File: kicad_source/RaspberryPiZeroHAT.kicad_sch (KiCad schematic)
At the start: 45 parts, among them CN1 RASPI-IO, CN2 WE_691210910004, CN3 SPE-T1-STRM-90, CN4 SPE-T1-STRM-90, SW1 SS-3235S-L3, U1 LAN8651, Y1 X1E0000210808

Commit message: glued project together
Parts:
- removed C1, C10, C4, C6, C7, C8, C9: 100nF, Capacitor_SMD:C_0603_1608Metric, symbol Device:C_Small
- removed C11, C12: 220nF, Capacitor_SMD:C_0603_1608Metric, symbol Device:C_Small
- removed C13, C14: 10 uF, Capacitor_SMD:C_0603_1608Metric, symbol Device:C_Small
- removed C2, C3: 22pF, Capacitor_SMD:C_0603_1608Metric, symbol Device:C_Small
- removed C5: 4.7 uF, Capacitor_SMD:C_0603_1608Metric, symbol Device:C_Small
- removed CN2: WE_691210910004, generationmake:WE_691210910004, symbol Connector_Generic:Conn_01x04
- removed CN3, CN4: SPE-T1-STRM-90, generationmake:SPE-T1-STRM-90, symbol Connector_Generic_MountingPin:Conn_01x02_MountingPin
- removed D5: DNI, Package_TO_SOT_SMD:SOT-23, symbol Power_Protection:NUP2105L
- removed FL1: ACT1210D-131-2P-TL00, generationmake:TDK_ACT1210D, symbol Device:Filter_EMI_LL_1423
- removed R10, R11, R14: 0R, Resistor_SMD:R_0603_1608Metric, symbol Device:R_Small
- removed R12: 12k4, Resistor_SMD:R_0603_1608Metric, symbol Device:R_Small
- removed R15, R16: 10k, Resistor_SMD:R_1206_3216Metric, symbol Device:R_Small
- removed R17, R4: 49R9, Resistor_SMD:R_1206_3216Metric, symbol Device:R_Small
- removed R18, R19: DNI, Resistor_SMD:R_0603_1608Metric, symbol Device:R_Small
- removed SW1: SS-3235S-L3, generationmake:SW_DPDT_XKB_SS-3235S-L3, symbol Switch:SW_DPDT_x2
- removed U1: LAN8651, Package_DFN_QFN:QFN-32-1EP_5x5mm_P0.5mm_EP3.45x3.45mm, symbol generationmake:LAN8651
- removed Y1: X1E0000210808, Crystal:Crystal_SMD_3225-4Pin_3.2x2.5mm, symbol CANFDZeroHAT-rescue:Crystal_SMD_4Pad-devices
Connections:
- net LAN8651_CS renamed LORA_CS
- net LAN8651_INT renamed LORA_INT
- no-connect marks 27 -> 15
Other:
- note added: "find the full project documentation at https://github.com/generationmake/LoRaZeroHAT"
- note removed: "130 uH @ 100 kHz"
- note removed: "25 MHz"
- note removed: "connectors according to Single Pair Ehernet System Alliance https://singlepairethernet.com/en/product-overview/connectors/"
- note removed: "find the full project documentation at https://github.com/generationmake/T1SZeroHAT"
- note removed: "no sleep mode supported by power supply!"
- note removed: "use NUP2105L or PESD2CAN"
- title: T1SZeroHAT -> LoRaZeroHAT
- moved on the sheet: CN1, R1, R13, R2, R3, R5, R6, R7, R8, R9

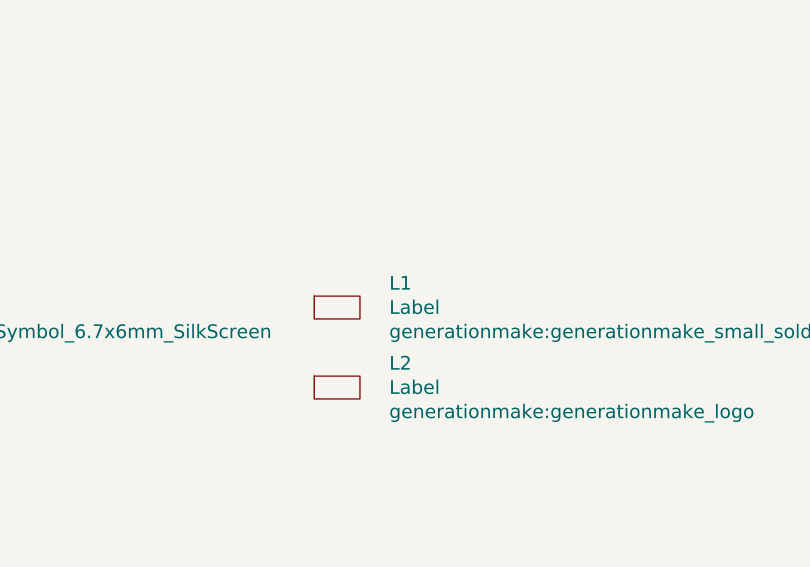
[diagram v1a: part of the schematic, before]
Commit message: connected schematic to layout
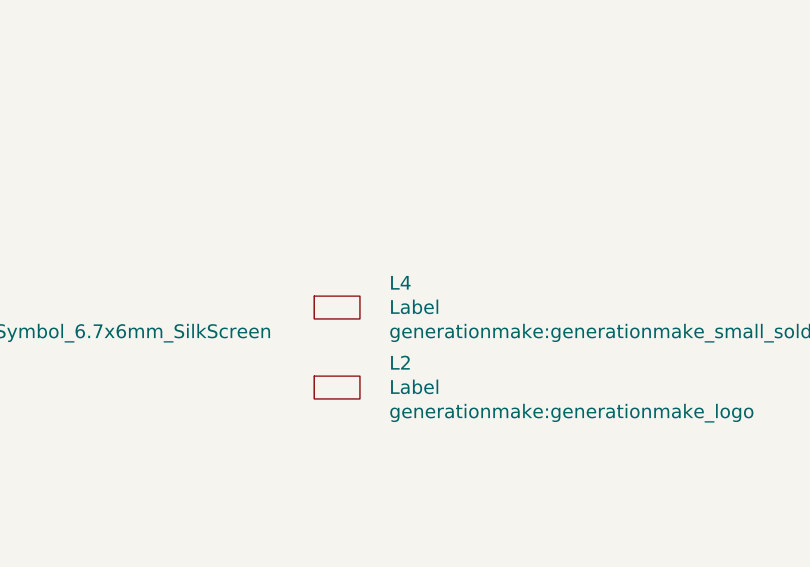
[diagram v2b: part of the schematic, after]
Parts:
- renumbered L1 to L4
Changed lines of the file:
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@@
 		(on_board yes)
 		(dnp no)
-		(property "Reference" "L1"
+		(property "Reference" "L4"
 			(at 240.7412 148.4376 0)
 			(effects
@@
 			(project ""
 				(path "/143f7a5b-9016-4d2c-b741-f535648590f8/54c42ff6-2a37-4707-b2a6-79c1a2f41127"
-					(reference "L1")
+					(reference "L4")
 					(unit 1)
 				)

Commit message: made first connections
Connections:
- net LORA_DIO0: now reaches CN1.29 (BCM5)
- net LORA_RESET: now reaches CN1.31 (BCM6)
- net SPI_CLK renamed SPI_SCK
- no-connect marks 15 -> 13
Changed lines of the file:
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@@
-	)
-	(no_connect
-		(at 68.58 168.91)
 	)
 	(no_connect
@@
 	)
 	(no_connect
-		(at 68.58 171.45)
-	)
-	(no_connect
 		(at 68.58 166.37)
 	)
@@
 	(wire
 		(pts
+			(xy 68.58 168.91) (xy 53.34 168.91)
+		)
+		(stroke
+			(width 0)
+			(type default)
+		)
+	)
+	(wire
+		(pts
 			(xy 72.39 113.03) (xy 74.93 113.03)
 		)
@@
 	(wire
 		(pts
+			(xy 53.34 177.8) (xy 41.91 177.8)
+		)
+		(stroke
+			(width 0)
+			(type default)
+		)
+	)
+	(wire
+		(pts
 			(xy 41.91 156.21) (xy 68.58 156.21)
 		)
@@
 	(wire
 		(pts
+			(xy 55.88 171.45) (xy 55.88 180.34)
+		)
+		(stroke
+			(width 0)
+			(type default)
+		)
+	)
+	(wire
+		(pts
 			(xy 66.04 181.61) (xy 66.04 184.15)
 		)
@@
 	(wire
 		(pts
+			(xy 55.88 180.34) (xy 41.91 180.34)
+		)
+		(stroke
+			(width 0)
+			(type default)
+		)
+	)
+	(wire
+		(pts
 			(xy 68.58 163.83) (xy 66.04 163.83)
 		)
@@
 	(wire
 		(pts
+			(xy 53.34 168.91) (xy 53.34 177.8)
+		)
+		(stroke
+			(width 0)
+			(type default)
+		)
+	)
+	(wire
+		(pts
 			(xy 74.93 100.33) (xy 74.93 106.68)
+		)
+		(stroke
+			(width 0)
+			(type default)
+		)
+	)
+	(wire
+		(pts
+			(xy 68.58 171.45) (xy 55.88 171.45)
 		)
 		(stroke
@@
 		)
 	)
-	(label "SPI_CLK"
+	(label "SPI_SCK"
 		(at 48.26 161.29 0)
 		(effects
@@
 		)
 	)
-	(global_label "SPI_CLK"
+	(global_label "LORA_RESET"
+		(shape output)
+		(at 41.91 180.34 180)
+		(fields_autoplaced yes)
+		(effects
+			(font
+				(size 1.27 1.27)
+			)
+			(justify right)
+		)
+		(property "Intersheetrefs" "${INTERSHEET_REFS}"
+			(at 27.4949 180.34 0)
+			(effects
+				(font
+					(size 1.27 1.27)
+				)
+				(justify right)
+				(hide yes)
+			)
+		)
+	)
+	(global_label "SPI_SCK"
 		(shape output)
 		(at 41.91 161.29 180)
@@
 		)
 		(property "Intersheetrefs" "${INTERSHEET_REFS}"
-			(at 31.3048 161.29 0)
+			(at 31.1234 161.29 0)
 			(effects
 				(font
@@
 				(hide yes)
 			)
+		)
+	)
+	(global_label "LORA_DIO0"
+		(shape input)
+		(at 41.91 177.8 180)
+		(fields_autoplaced yes)
+		(effects
+			(font
+				(size 1.27 1.27)
+			)
+			(justify right)
+		)
+		(property "Intersheetrefs" "${INTERSHEET_REFS}"
+			(at 28.8252 177.8 0)
+			(effects
+				(font
+					(size 1.27 1.27)
+				)
+				(justify right)
+				(hide yes)
+			)

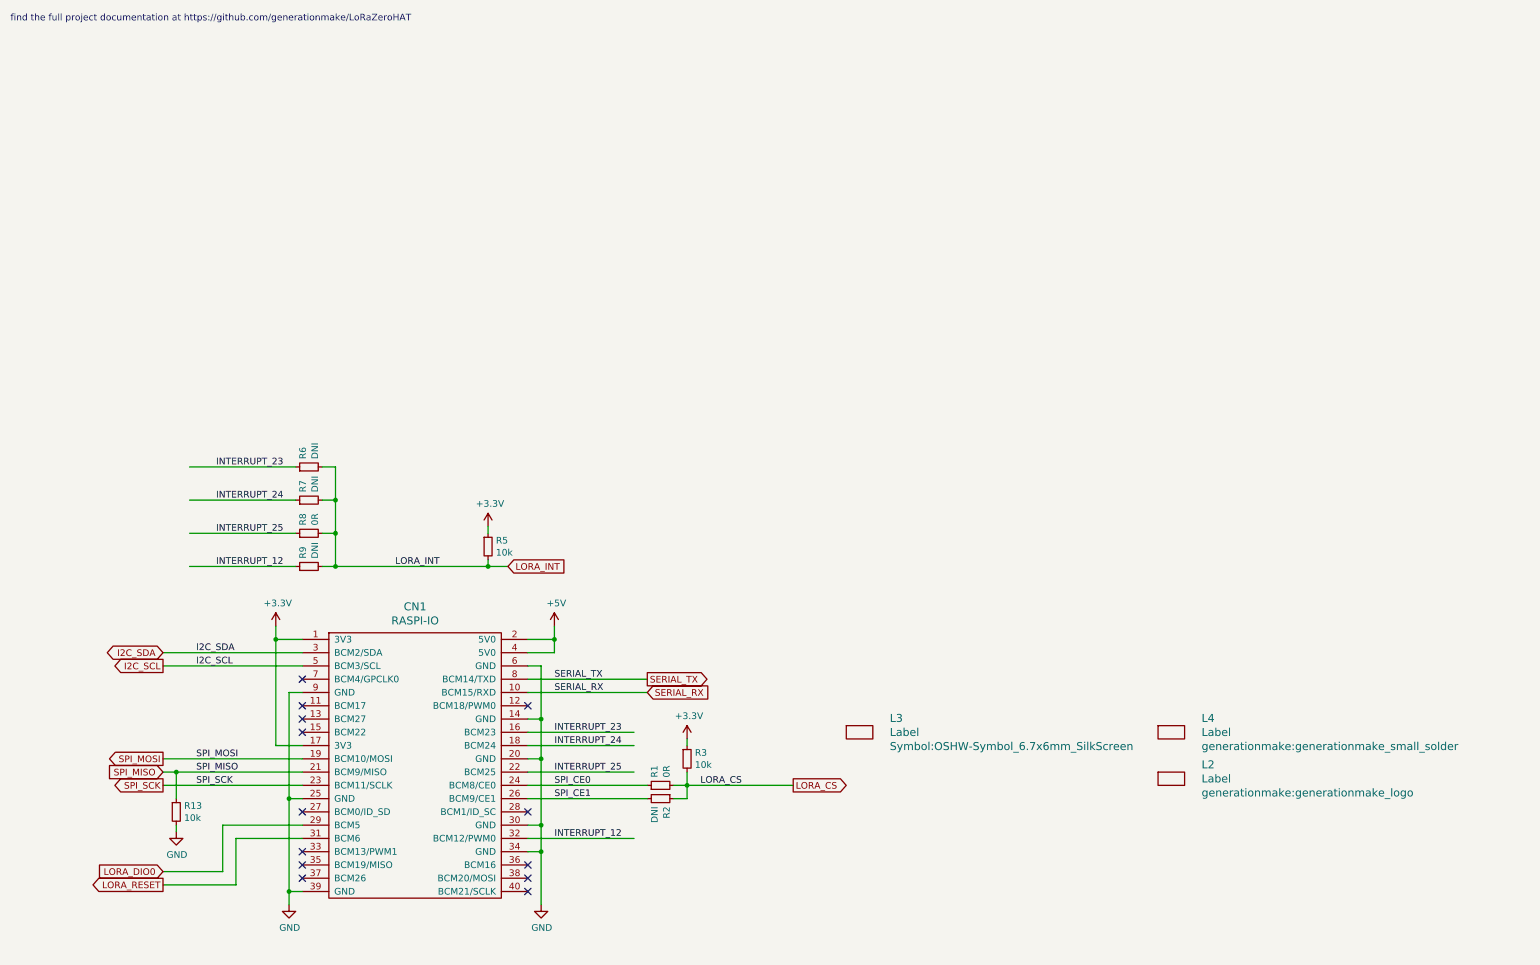
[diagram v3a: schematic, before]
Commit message: updated layout
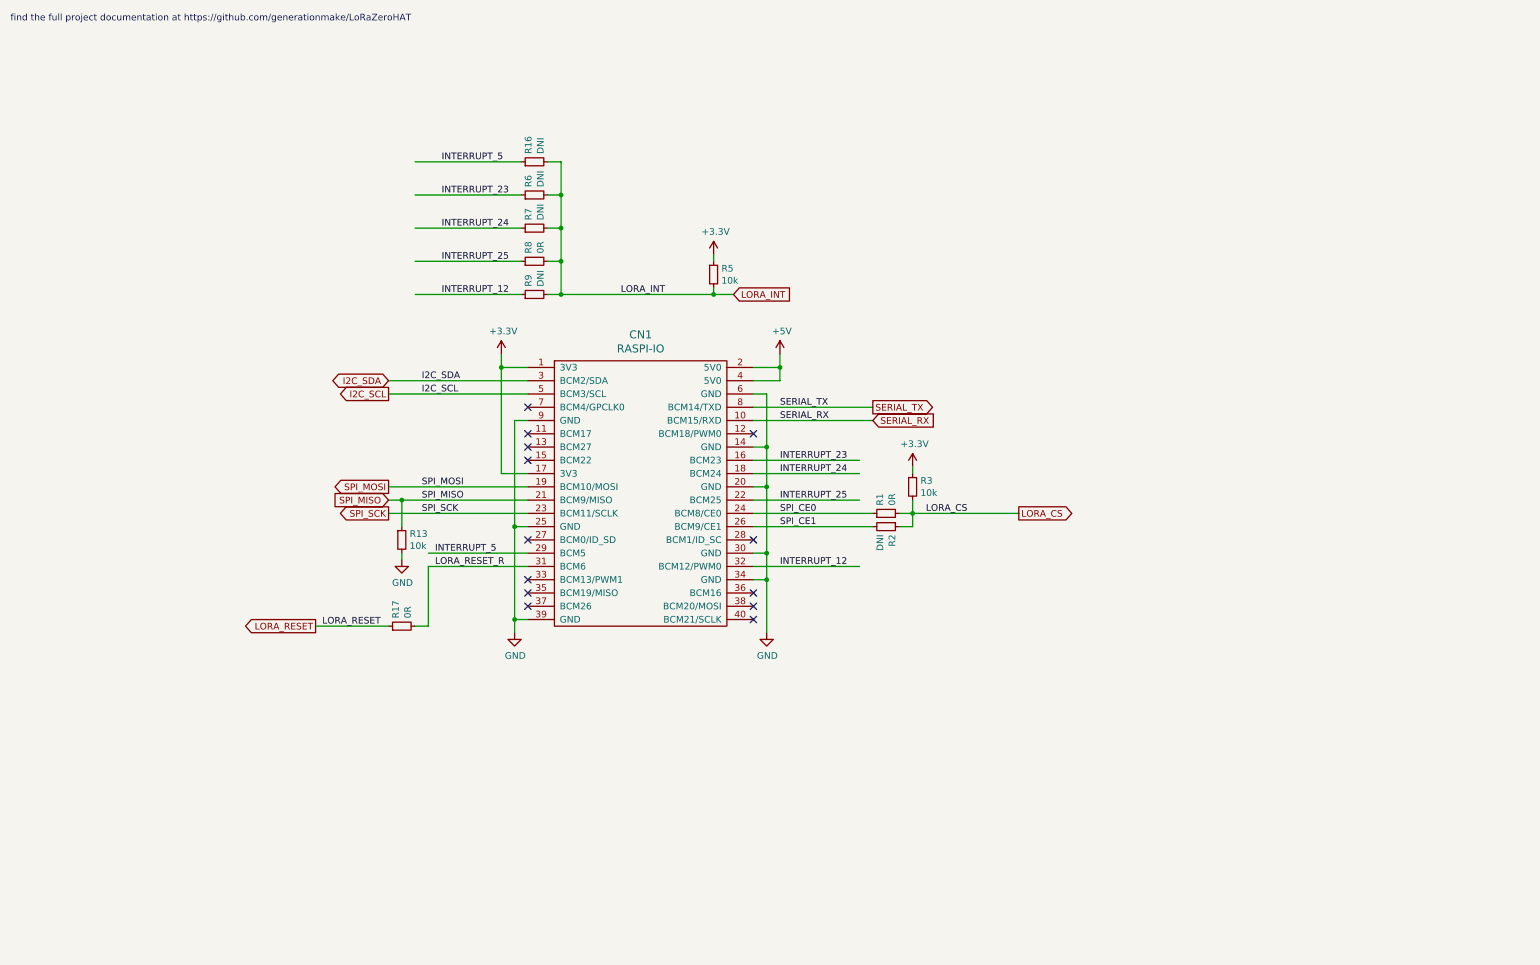
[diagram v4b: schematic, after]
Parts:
- removed L2: Label, generationmake:generationmake_logo, symbol generationmake:Label
- removed L3: Label, Symbol:OSHW-Symbol_6.7x6mm_SilkScreen, symbol generationmake:Label
- removed L4: Label, generationmake:generationmake_small_solder, symbol generationmake:Label
- added R16: DNI, Resistor_SMD:R_0603_1608Metric, symbol Device:R_Small
- added R17: 0R, Resistor_SMD:R_0603_1608Metric, symbol Device:R_Small
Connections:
- net LORA_INT: now also R16.2
- net LORA_RESET: now also R17.1; no longer CN1.31 (BCM6)
- net LORA_DIO0 renamed INTERRUPT_5
- net INTERRUPT_5: now also R16.1
- new net LORA_RESET_R: CN1.31 (BCM6), R17.2
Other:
- moved on the sheet: CN1, R1, R13, R2, R3, R5, R6, R7, R8, R9

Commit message: schaltplan neu annotiert
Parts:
- renumbered R13 to R1, R2 to R10, R3 to R11, R17 to R2, R16 to R3, R6 to R4, R7 to R5, R8 to R6, R9 to R7, R5 to R8, R1 to R9
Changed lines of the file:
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@@
 		(on_board yes)
 		(dnp no)
-		(property "Reference" "#PWR0101"
+		(property "Reference" "#PWR2"
 			(at 106.68 82.55 0)
 			(effects
@@
 			(project ""
 				(path "/143f7a5b-9016-4d2c-b741-f535648590f8/54c42ff6-2a37-4707-b2a6-79c1a2f41127"
-					(reference "#PWR0101")
+					(reference "#PWR2")
 					(unit 1)
 				)
@@
 		(on_board yes)
 		(dnp no)
-		(property "Reference" "#PWR0102"
+		(property "Reference" "#PWR3"
 			(at 109.22 138.43 0)
 			(effects
@@
 			(project ""
 				(path "/143f7a5b-9016-4d2c-b741-f535648590f8/54c42ff6-2a37-4707-b2a6-79c1a2f41127"
-					(reference "#PWR0102")
+					(reference "#PWR3")
 					(unit 1)
 				)
@@
 		(on_board yes)
 		(dnp no)
-		(property "Reference" "#PWR0103"
+		(property "Reference" "#PWR5"
 			(at 157.48 138.43 0)
 			(effects
@@
 			(project ""
 				(path "/143f7a5b-9016-4d2c-b741-f535648590f8/54c42ff6-2a37-4707-b2a6-79c1a2f41127"
-					(reference "#PWR0103")
+					(reference "#PWR5")
 					(unit 1)
 				)
@@
 		(on_board yes)
 		(dnp no)
-		(property "Reference" "#PWR0104"
+		(property "Reference" "#PWR6"
 			(at 160.02 82.55 0)
 			(effects
@@
 			(project ""
 				(path "/143f7a5b-9016-4d2c-b741-f535648590f8/54c42ff6-2a37-4707-b2a6-79c1a2f41127"
-					(reference "#PWR0104")
+					(reference "#PWR6")
 					(unit 1)
 				)
@@
 		(on_board yes)
 		(dnp no)
-		(property "Reference" "R3"
+		(property "Reference" "R11"
 			(at 186.9186 102.9716 0)
 			(effects
@@
 			(project ""
 				(path "/143f7a5b-9016-4d2c-b741-f535648590f8/54c42ff6-2a37-4707-b2a6-79c1a2f41127"
-					(reference "R3")
+					(reference "R11")
 					(unit 1)
 				)
@@
 		(on_board yes)
 		(dnp no)
-		(property "Reference" "#PWR010"
+		(property "Reference" "#PWR7"
 			(at 185.42 104.14 0)
 			(effects
@@
 			(project ""
 				(path "/143f7a5b-9016-4d2c-b741-f535648590f8/54c42ff6-2a37-4707-b2a6-79c1a2f41127"
-					(reference "#PWR010")
+					(reference "#PWR7")
 					(unit 1)
 				)
@@
 		(on_board yes)
 		(dnp no)
-		(property "Reference" "R1"
+		(property "Reference" "R9"
 			(at 179.1716 107.7214 0)
 			(effects
@@
 			(project ""
 				(path "/143f7a5b-9016-4d2c-b741-f535648590f8/54c42ff6-2a37-4707-b2a6-79c1a2f41127"
-					(reference "R1")
+					(reference "R9")
 					(unit 1)
 				)
@@
 		(on_board yes)
 		(dnp no)
-		(property "Reference" "R2"
+		(property "Reference" "R10"
 			(at 181.5084 113.2586 0)
 			(effects
@@
 			(project ""
 				(path "/143f7a5b-9016-4d2c-b741-f535648590f8/54c42ff6-2a37-4707-b2a6-79c1a2f41127"
-					(reference "R2")
+					(reference "R10")
 					(unit 1)
 				)
@@
 		(on_board yes)
 		(dnp no)
-		(property "Reference" "R5"
+		(property "Reference" "R8"
 			(at 148.8186 62.3316 0)
 			(effects
@@
 			(project ""
 				(path "/143f7a5b-9016-4d2c-b741-f535648590f8/54c42ff6-2a37-4707-b2a6-79c1a2f41127"
-					(reference "R5")
+					(reference "R8")
 					(unit 1)
 				)
@@
 		(on_board yes)
 		(dnp no)
-		(property "Reference" "#PWR011"
+		(property "Reference" "#PWR4"
 			(at 147.32 63.5 0)
 			(effects
@@
 			(project ""
 				(path "/143f7a5b-9016-4d2c-b741-f535648590f8/54c42ff6-2a37-4707-b2a6-79c1a2f41127"
-					(reference "#PWR011")
+					(reference "#PWR4")
 					(unit 1)
 				)
@@
 		(on_board yes)
 		(dnp no)
-		(property "Reference" "R9"
+		(property "Reference" "R7"
 			(at 111.8616 65.8114 0)
 			(effects
@@
 			(project ""
 				(path "/143f7a5b-9016-4d2c-b741-f535648590f8/54c42ff6-2a37-4707-b2a6-79c1a2f41127"
-					(reference "R9")
+					(reference "R7")
 					(unit 1)
 				)
@@
 		(on_board yes)
 		(dnp no)
-		(property "Reference" "R8"
+		(property "Reference" "R6"
 			(at 111.8616 59.4614 0)
 			(effects
@@
 			(project ""
 				(path "/143f7a5b-9016-4d2c-b741-f535648590f8/54c42ff6-2a37-4707-b2a6-79c1a2f41127"
-					(reference "R8")
+					(reference "R6")
 					(unit 1)
 				)
@@
 		(on_board yes)
 		(dnp no)
-		(property "Reference" "R7"
+		(property "Reference" "R5"
 			(at 111.8616 53.1114 0)
 			(effects
@@
 			(project ""
 				(path "/143f7a5b-9016-4d2c-b741-f535648590f8/54c42ff6-2a37-4707-b2a6-79c1a2f41127"
-					(reference "R7")
+					(reference "R5")
 					(unit 1)
 				)
@@
 		(on_board yes)
 		(dnp no)
-		(property "Reference" "R6"
+		(property "Reference" "R4"
 			(at 111.8616 46.7614 0)
 			(effects
@@
 			(project ""
 				(path "/143f7a5b-9016-4d2c-b741-f535648590f8/54c42ff6-2a37-4707-b2a6-79c1a2f41127"
-					(reference "R6")
+					(reference "R4")
 					(unit 1)
 				)
@@
 		(on_board yes)
 		(dnp no)
-		(property "Reference" "R16"
+		(property "Reference" "R3"
 			(at 111.8616 40.4114 0)
 			(effects
@@
 			(project "LoRaZeroHAT"
 				(path "/143f7a5b-9016-4d2c-b741-f535648590f8/54c42ff6-2a37-4707-b2a6-79c1a2f41127"
-					(reference "R16")
+					(reference "R3")
 					(unit 1)
 				)
@@
 		(on_board yes)
 		(dnp no)
-		(property "Reference" "R17"
+		(property "Reference" "R2"
 			(at 86.4616 129.3114 0)
 			(effects
@@
 			(project "LoRaZeroHAT"
 				(path "/143f7a5b-9016-4d2c-b741-f535648590f8/54c42ff6-2a37-4707-b2a6-79c1a2f41127"
-					(reference "R17")
+					(reference "R2")
 					(unit 1)
 				)
@@
 		(on_board yes)
 		(dnp no)
-		(property "Reference" "#PWR019"
+		(property "Reference" "#PWR1"
 			(at 87.63 124.46 0)
 			(effects
@@
 			(project ""
 				(path "/143f7a5b-9016-4d2c-b741-f535648590f8/54c42ff6-2a37-4707-b2a6-79c1a2f41127"
-					(reference "#PWR019")
+					(reference "#PWR1")
 					(unit 1)
 				)
@@
 		(on_board yes)
 		(dnp no)
-		(property "Reference" "R13"
+		(property "Reference" "R1"
 			(at 89.1286 113.1316 0)
 			(effects
@@
 			(project ""
 				(path "/143f7a5b-9016-4d2c-b741-f535648590f8/54c42ff6-2a37-4707-b2a6-79c1a2f41127"
-					(reference "R13")
-					(unit 1)
-				)
+					(reference "R1")
+					(unit 1)
+				)
